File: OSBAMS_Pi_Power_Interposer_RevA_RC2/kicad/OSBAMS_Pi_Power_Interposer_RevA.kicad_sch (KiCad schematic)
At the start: 2 parts, among them J1 43045-0400, J2 SSW-120-01-S-D

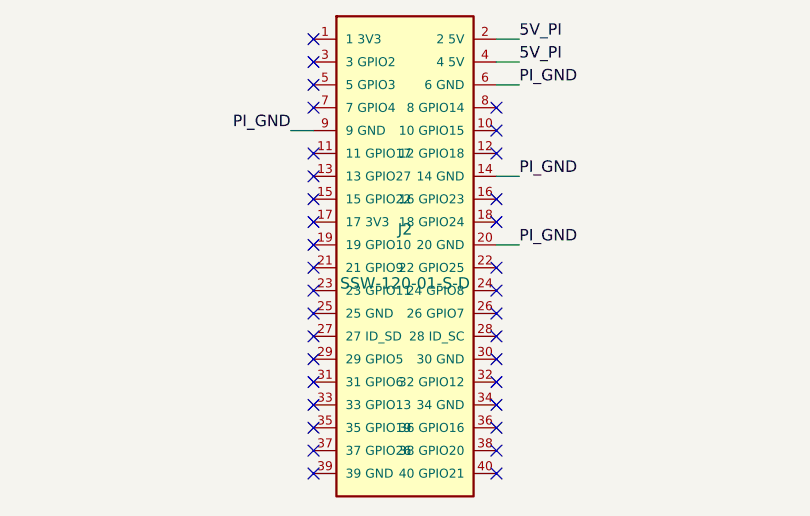
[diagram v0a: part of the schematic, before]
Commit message: Pi power RC2: close source items - Waveshare data, Molex 43030-0038 + 18 AWG harness (16 AWG invalid), SSW-120-01-L-D, SMBJ15A row; budget re-run
PCB/interposer geometry unchanged; ERC/DRC/parity 0 on both projects.

Co-Authored-By: Claude Sonnet 5.5 <noreply@anthropic.com>
Claude-Session: https://claude.ai/code/session_01ENatZXrEDA18PaxUrZWrpi
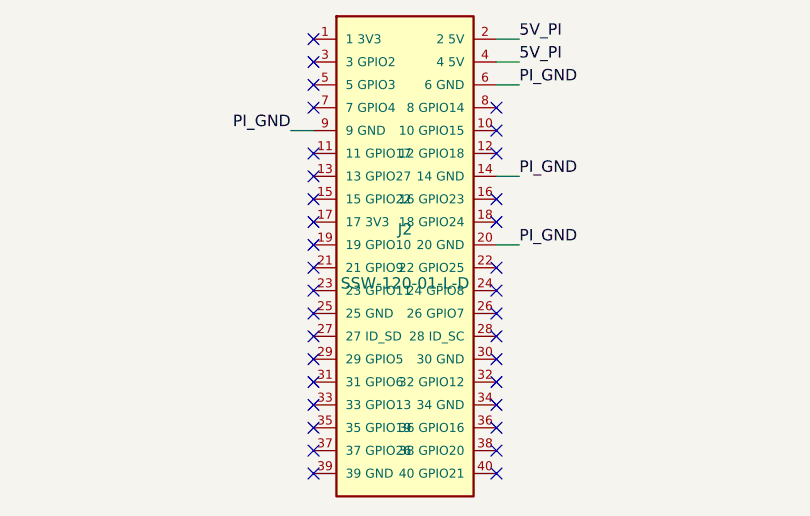
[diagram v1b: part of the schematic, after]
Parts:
- J2: value SSW-120-01-S-D -> SSW-120-01-L-D; footprint OSBAMS_PiPwr:SSW-120-01-S-D_RPi_TopView -> OSBAMS_PiPwr:SSW-120-01-L-D_RPi_TopView; MPN SSW-120-01-S-D -> SSW-120-01-L-D
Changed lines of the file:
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@@
 (symbol (lib_id "OSBAMS_PiPwr:RPi40") (at 129.54 149.86 0) (unit 1) (in_bom yes) (on_board yes) (dnp no)
   (property "Reference" "J2" (at 129.54 146.86 0) (effects (font (size 1.27 1.27))))
-  (property "Value" "SSW-120-01-S-D" (at 129.54 152.86 0) (effects (font (size 1.27 1.27))))
-  (property "Footprint" "OSBAMS_PiPwr:SSW-120-01-S-D_RPi_TopView" (at 129.54 149.86 0) (effects hide))
+  (property "Value" "SSW-120-01-L-D" (at 129.54 152.86 0) (effects (font (size 1.27 1.27))))
+  (property "Footprint" "OSBAMS_PiPwr:SSW-120-01-L-D_RPi_TopView" (at 129.54 149.86 0) (effects hide))
   (property "Datasheet" "" (at 129.54 149.86 0) (effects hide))
-  (property "MPN" "SSW-120-01-S-D" (at 129.54 149.86 0) (effects hide))
+  (property "MPN" "SSW-120-01-L-D" (at 129.54 149.86 0) (effects hide))
   (pin "1")(pin "3")(pin "5")(pin "7")(pin "9")(pin "11")(pin "13")(pin "15")(pin "17")(pin "19")(pin "21")(pin "23")(pin "25")(pin "27")(pin "29")(pin "31")(pin "33")(pin "35")(pin "37")(pin "39")(pin "2")(pin "4")(pin "6")(pin "8")(pin "10")(pin "12")(pin "14")(pin "16")(pin "18")(pin "20")(pin "22")(pin "24")(pin "26")(pin "28")(pin "30")(pin "32")(pin "34")(pin "36")(pin "38")(pin "40")
   (instances (project "OSBAMS_Pi_Power_Interposer_RevA" (path "/3b1d6c7e-2a44-4f0e-8d5a-91c0a7e4b002" (reference "J2") (unit 1)))))
